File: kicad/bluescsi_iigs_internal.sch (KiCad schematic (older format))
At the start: 27 parts, among them J1 Conn_02x13_Odd_Even, J2 Conn_02x13_Odd_Even, J3 105162-0001, J4 Conn_01x02_Male, J5 Conn_01x02_Male, M1 Screw_Terminal_01x01, M2 Screw_Terminal_01x01, Q1 Q_PMOS_GSD, SW1 SW_SPDT, U1 YAAJ_BluePill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

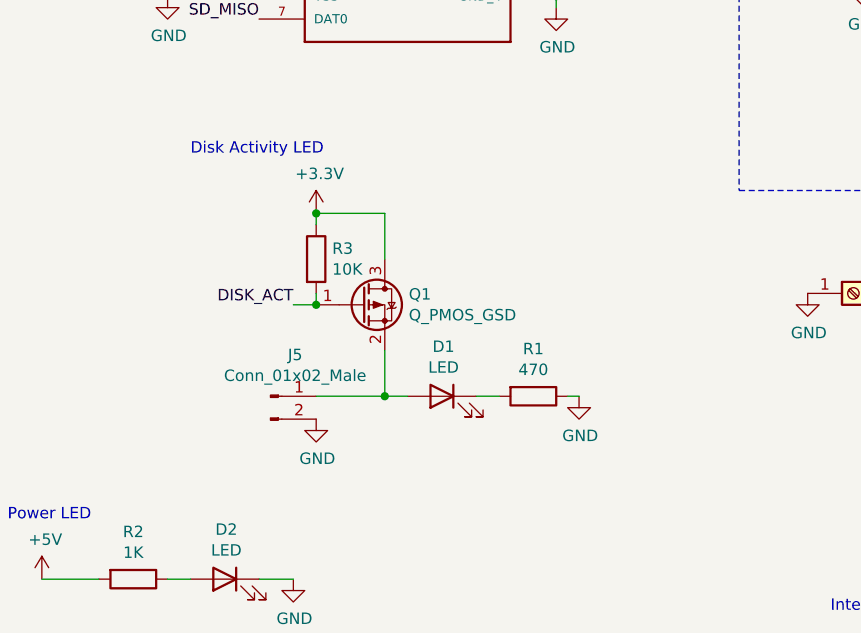
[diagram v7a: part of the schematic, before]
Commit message: replace lef mostfest with logic inverter
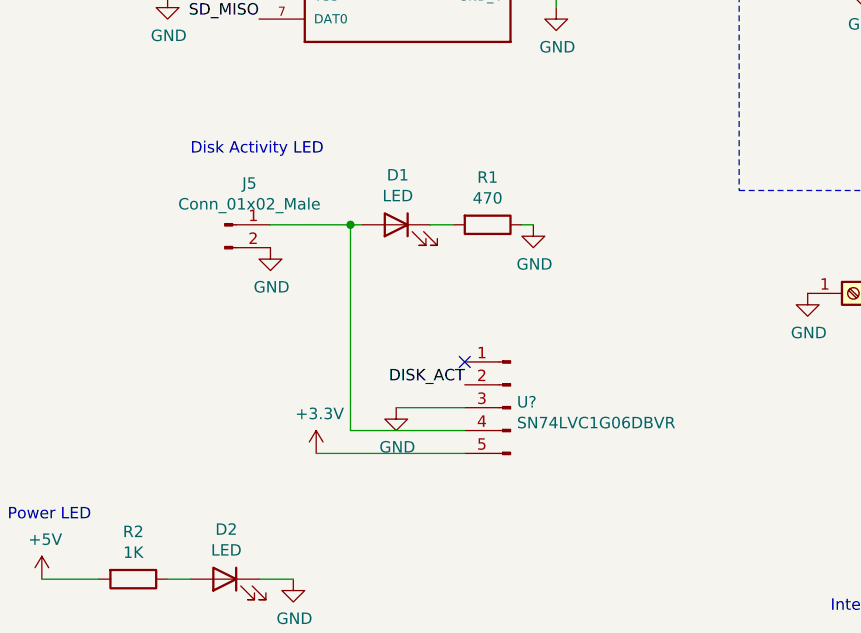
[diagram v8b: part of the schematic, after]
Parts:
- removed Q1: Q_PMOS_GSD, Package_TO_SOT_SMD:SOT-23, symbol Device:Q_PMOS_GSD
- removed R3: 10K, Resistor_SMD:R_0805_2012Metric_Pad1.20x1.40mm_HandSolder, symbol Device:R
- added U?: SN74LVC1G06DBVR, Package_TO_SOT_SMD:SOT-23-5_HandSoldering, symbol Connector:Conn_01x05_Male
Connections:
- net +3V3: now also U?.5 (Pin_5)
- net DISK_ACT: now also U?.2 (Pin_2)
- net GND: now also U?.3 (Pin_3)
- net at D1.2 (A), J5.1 (Pin_1): now also U?.4 (Pin_4)
- no-connect marks 13 -> 14
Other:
- moved on the sheet: D1, J5, R1
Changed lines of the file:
@@
 Wire Wire Line
 	4450 7350 4550 7350
-Text Label 5000 6150 2    50   ~ 0
-DISK_ACT
 $Comp
 L Device:R R1
 U 1 1 606332E3
-P 6050 6550
-F 0 "R1" V 5843 6550 50  0000 C CNN
-F 1 "470" V 5934 6550 50  0000 C CNN
-F 2 "Resistor_SMD:R_0805_2012Metric_Pad1.20x1.40mm_HandSolder" V 5980 6550 50  0001 C CNN
-F 3 "~" H 6050 6550 50  0001 C CNN
-	1    6050 6550
+P 5850 5800
+F 0 "R1" V 5643 5800 50  0000 C CNN
+F 1 "470" V 5734 5800 50  0000 C CNN
+F 2 "Resistor_SMD:R_0805_2012Metric_Pad1.20x1.40mm_HandSolder" V 5780 5800 50  0001 C CNN
+F 3 "~" H 5850 5800 50  0001 C CNN
+	1    5850 5800
 	0    1    1    0
-$EndComp
-$Comp
-L Device:LED D1
-U 1 1 60632077
-P 5650 6550
-F 0 "D1" H 5643 6767 50  0000 C CNN
-F 1 "LED" H 5643 6676 50  0000 C CNN
-F 2 "LED_SMD:LED_0805_2012Metric_Pad1.15x1.40mm_HandSolder" H 5650 6550 50  0001 C CNN
-F 3 "~" H 5650 6550 50  0001 C CNN
-	1    5650 6550
-	-1   0    0    -1
 $EndComp
 Text Notes 4550 5500 0    50   ~ 0
@@
 Wire Wire Line
 	4400 1700 4850 1700
-$Comp
-L Device:Q_PMOS_GSD Q1
-U 1 1 609D8A80
-P 5300 6150
-F 0 "Q1" H 5505 6196 50  0000 L CNN
-F 1 "Q_PMOS_GSD" H 5505 6105 50  0000 L CNN
-F 2 "Package_TO_SOT_SMD:SOT-23" H 5500 6250 50  0001 C CNN
-F 3 "~" H 5300 6150 50  0001 C CNN
-	1    5300 6150
-	1    0    0    -1
-$EndComp
-$Comp
-L power:+3.3V #PWR0126
-U 1 1 609DCA9E
-P 5100 5750
-F 0 "#PWR0126" H 5100 5600 50  0001 C CNN
-F 1 "+3.3V" H 5115 5923 50  0000 C CNN
-F 2 "" H 5100 5750 50  0001 C CNN
-F 3 "" H 5100 5750 50  0001 C CNN
-	1    5100 5750
-	1    0    0    -1
-$EndComp
-$Comp
-L Device:R R3
-U 1 1 609DE44B
-P 5100 5950
-F 0 "R3" H 5170 5996 50  0000 L CNN
-F 1 "10K" H 5170 5905 50  0000 L CNN
-F 2 "Resistor_SMD:R_0805_2012Metric_Pad1.20x1.40mm_HandSolder" V 5030 5950 50  0001 C CNN
-F 3 "~" H 5100 5950 50  0001 C CNN
-	1    5100 5950
-	1    0    0    -1
-$EndComp
-Wire Wire Line
-	5100 5750 5400 5750
-Wire Wire Line
-	5000 6150 5100 6150
-Wire Wire Line
-	5400 6550 5500 6550
-Wire Wire Line
-	5400 6350 5400 6550
-Wire Wire Line
-	5800 6550 5900 6550
+Wire Wire Line
+	5600 5800 5700 5800
 $Comp
 L power:GND #PWR0127
 U 1 1 609F55CD
-P 6250 6550
-F 0 "#PWR0127" H 6250 6300 50  0001 C CNN
-F 1 "GND" H 6255 6377 50  0000 C CNN
-F 2 "" H 6250 6550 50  0001 C CNN
-F 3 "" H 6250 6550 50  0001 C CNN
-	1    6250 6550
-	1    0    0    -1
-$EndComp
-Wire Wire Line
-	6200 6550 6250 6550
-Wire Wire Line
-	5400 5750 5400 5950
-Wire Wire Line
-	5100 5750 5100 5800
-Connection ~ 5100 5750
-Wire Wire Line
-	5100 6100 5100 6150
-Connection ~ 5100 6150
+P 6050 5800
+F 0 "#PWR0127" H 6050 5550 50  0001 C CNN
+F 1 "GND" H 6055 5627 50  0000 C CNN
+F 2 "" H 6050 5800 50  0001 C CNN
+F 3 "" H 6050 5800 50  0001 C CNN
+	1    6050 5800
+	1    0    0    -1
+$EndComp
+Wire Wire Line
+	6000 5800 6050 5800
 $Comp
 L Connector:Conn_01x02_Male J5
 U 1 1 60AA760E
-P 4900 6550
-F 0 "J5" H 5008 6731 50  0000 C CNN
-F 1 "Conn_01x02_Male" H 5008 6640 50  0000 C CNN
-F 2 "Connector_PinHeader_2.54mm:PinHeader_1x02_P2.54mm_Vertical" H 4900 6550 50  0001 C CNN
-F 3 "~" H 4900 6550 50  0001 C CNN
-	1    4900 6550
-	1    0    0    -1
-$EndComp
-Wire Wire Line
-	5100 6550 5400 6550
-Connection ~ 5400 6550
+P 4700 5800
+F 0 "J5" H 4808 5981 50  0000 C CNN
+F 1 "Conn_01x02_Male" H 4808 5890 50  0000 C CNN
+F 2 "Connector_PinHeader_2.54mm:PinHeader_1x02_P2.54mm_Vertical" H 4700 5800 50  0001 C CNN
+F 3 "~" H 4700 5800 50  0001 C CNN
+	1    4700 5800
+	1    0    0    -1
+$EndComp
 $Comp
 L power:GND #PWR0128
 U 1 1 60AA99DB
-P 5100 6650
-F 0 "#PWR0128" H 5100 6400 50  0001 C CNN
-F 1 "GND" H 5105 6477 50  0000 C CNN
-F 2 "" H 5100 6650 50  0001 C CNN
-F 3 "" H 5100 6650 50  0001 C CNN
-	1    5100 6650
+P 4900 5900
+F 0 "#PWR0128" H 4900 5650 50  0001 C CNN
+F 1 "GND" H 4905 5727 50  0000 C CNN
+F 2 "" H 4900 5900 50  0001 C CNN
+F 3 "" H 4900 5900 50  0001 C CNN
+	1    4900 5900
 	1    0    0    -1
 $EndComp
@@
 	1    0    0    -1
 $EndComp
+$Comp
+L Connector:Conn_01x05_Male U?
+U 1 1 60C23A85
+P 5950 6600
+F 0 "U?" H 5922 6624 50  0000 R CNN
+F 1 "SN74LVC1G06DBVR" H 5922 6533 50  0000 R CNN
+F 2 "Package_TO_SOT_SMD:SOT-23-5_HandSoldering" H 5950 6600 50  0001 C CNN
+F 3 "https://www.mouser.com/datasheet/2/308/1/NL17SZ07_D-2318022.pdf" H 5950 6600 50  0001 C CNN
+	1    5950 6600
+	-1   0    0    -1
+$EndComp
+NoConn ~ 5750 6400
+Text Label 5750 6500 2    50   ~ 0
+DISK_ACT
+$Comp
+L power:GND #PWR?
+U 1 1 60C2A0B7
+P 5450 6600
+F 0 "#PWR?" H 5450 6350 50  0001 C CNN
+F 1 "GND" H 5455 6427 50  0000 C CNN
+F 2 "" H 5450 6600 50  0001 C CNN
+F 3 "" H 5450 6600 50  0001 C CNN
+	1    5450 6600
+	1    0    0    -1
+$EndComp
+Wire Wire Line
+	5750 6600 5450 6600
+$Comp
+L power:+3.3V #PWR?
+U 1 1 60C2CD62
+P 5100 6800
+F 0 "#PWR?" H 5100 6650 50  0001 C CNN
+F 1 "+3.3V" H 5115 6973 50  0000 C CNN
+F 2 "" H 5100 6800 50  0001 C CNN
+F 3 "" H 5100 6800 50  0001 C CNN
+	1    5100 6800
+	1    0    0    -1
+$EndComp
+Wire Wire Line
+	5100 6800 5750 6800
+Wire Wire Line
+	5750 6700 5250 6700
+Wire Wire Line
+	5250 6700 5250 5800
+Connection ~ 5250 5800
+Wire Wire Line
+	5250 5800 5300 5800
+Wire Wire Line
+	4900 5800 5250 5800
+$Comp
+L Device:LED D1
+U 1 1 60632077
+P 5450 5800
+F 0 "D1" H 5443 6017 50  0000 C CNN
+F 1 "LED" H 5443 5926 50  0000 C CNN
+F 2 "LED_SMD:LED_0805_2012Metric_Pad1.15x1.40mm_HandSolder" H 5450 5800 50  0001 C CNN
+F 3 "~" H 5450 5800 50  0001 C CNN
+	1    5450 5800
+	-1   0    0    -1
+$EndComp
 $EndSCHEMATC
